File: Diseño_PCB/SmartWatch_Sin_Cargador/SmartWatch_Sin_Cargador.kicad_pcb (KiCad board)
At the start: 2 copper layers, 45 x 45 mm, 19 parts, among them J1 FTDI, J2 Input_BAT, J3 Input_Charger, SW1 SW_Push, SW2 SW_Push, SW3 SW_Push_Dual, SW4 SW_Push_Dual, SW5 SW_Push_Dual, SW6 SW_SPST, U1 ESP-12F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

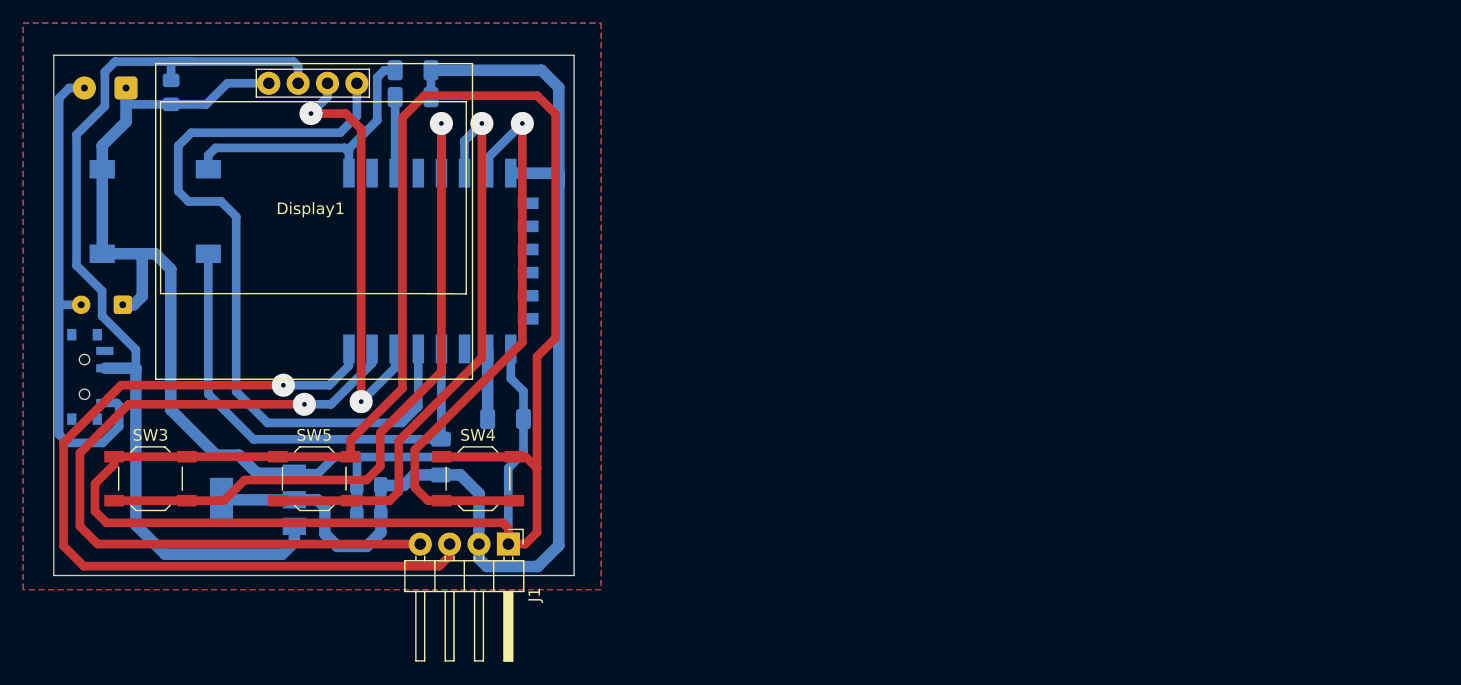
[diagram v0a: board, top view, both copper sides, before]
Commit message: Cree las carpetas de diseño 3D y actuaice el PCB del que no lleva cargador
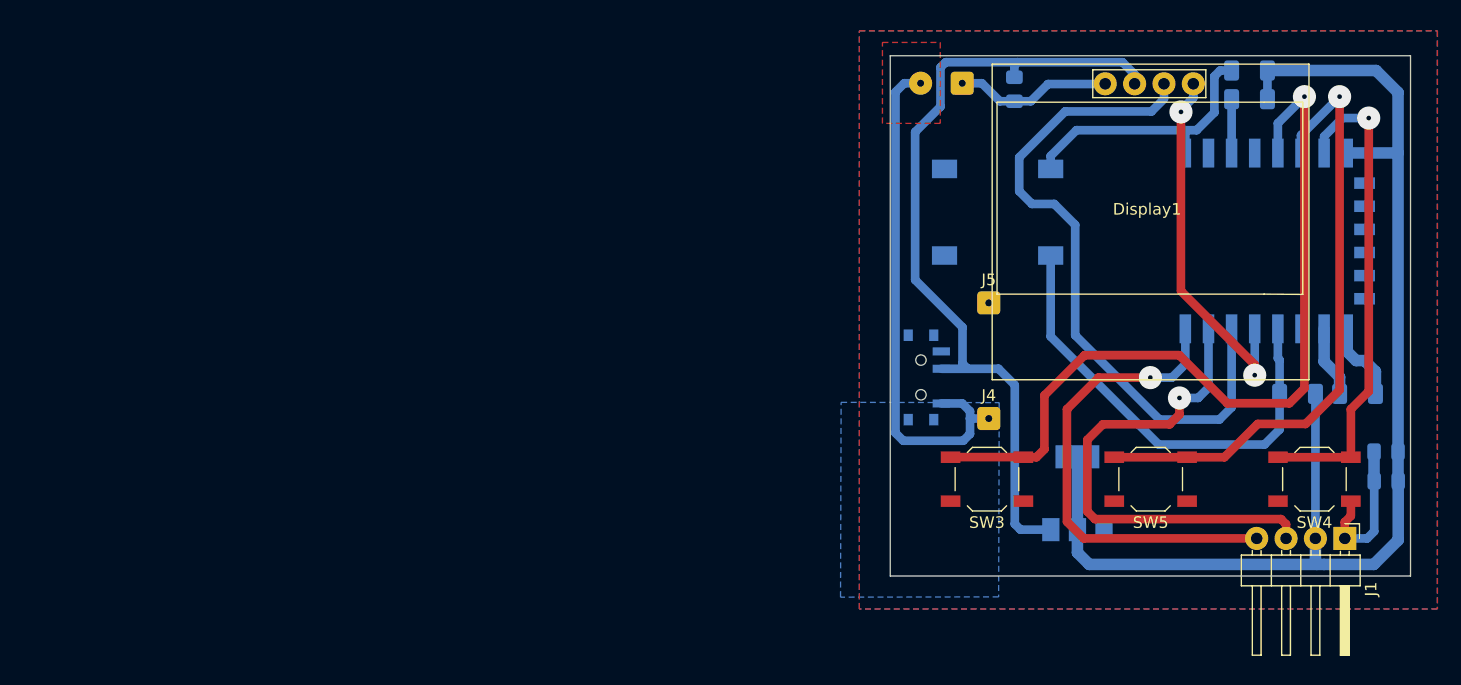
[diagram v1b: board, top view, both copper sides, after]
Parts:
- removed J3: Input_Charger, Connector_Wire:SolderWire-0.1sqmm_1x02_P3.6mm_D0.4mm_OD1mm
- added J4: Input_Charger++, Connector_Wire:SolderWire-0.1sqmm_1x01_D0.4mm_OD1mm, F.Cu at (164.5, 86.2)
- added J5: Input_Charger--, Connector_Wire:SolderWire-0.1sqmm_1x01_D0.4mm_OD1mm, F.Cu at (164.5, 76.2)
- moved C3 88.0 mm to (198.9, 91.6)
- moved C1 88.0 mm to (198.9, 89.1)
- moved R3 74.3 mm to (191.2, 84.1), turned to 180 degrees
- moved R4 73.7 mm to (196.4, 84.1)
- moved C2 72.9 mm to (166.7, 57.7)
- moved SW2 72.9 mm to (165.3, 72.1)
- moved SW1 72.9 mm to (165.3, 64.6)
- moved U1 72.4 mm to (185.0, 70.8)
- moved SW3 72.3 mm to (164.4, 91.4), turned to 180 degrees
- moved SW5 72.3 mm to (178.5, 91.4), turned to 180 degrees
- moved Display1 72.3 mm to (178.2, 67.8)
- moved SW4 72.3 mm to (192.7, 91.4), turned to 180 degrees
- moved J1 72.3 mm to (195.3, 96.6)
- moved R1 72.3 mm to (187.1, 58.6)
- moved SW6 72.3 mm to (159.0, 82.6)
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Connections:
- J1 pad 3: /Tx -> /Rx
- J1 pad 4: /Rx -> /Tx
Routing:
- net GND: track 267.2 -> 33.9 mm
- net /SDA: track 66.8 -> 32.3 mm, vias 0 -> 2
- net /Tx: track 73.3 -> 41.7 mm
- net /Rx: track 66.1 -> 43.3 mm
- net /SCL: track 37.5 -> 58.2 mm, vias 2 -> 0
- net /VCC_OLED: track 83.7 -> 70.8 mm
- net +3.3V: track 103.3 -> 113.8 mm
- net Net-(U1-GPIO14): track 60.4 -> 70.3 mm
- net Net-(U1-GPIO13): track 50.0 -> 42.2 mm
- net Net-(U1-GPIO12): track 50.5 -> 53.5 mm
- net /VBAT: track 42.9 -> 45.3 mm
- net Net-(U1-EN): track 6.58 -> 4.66 mm
- net Net-(U1-GPIO0): track 41.8 -> 40.0 mm
- net Net-(U1-~{RST}): track 24.9 -> 23.6 mm
- added copper zone on B.Cu, net /VBAT
- added copper zone on F.Cu, net /VBAT

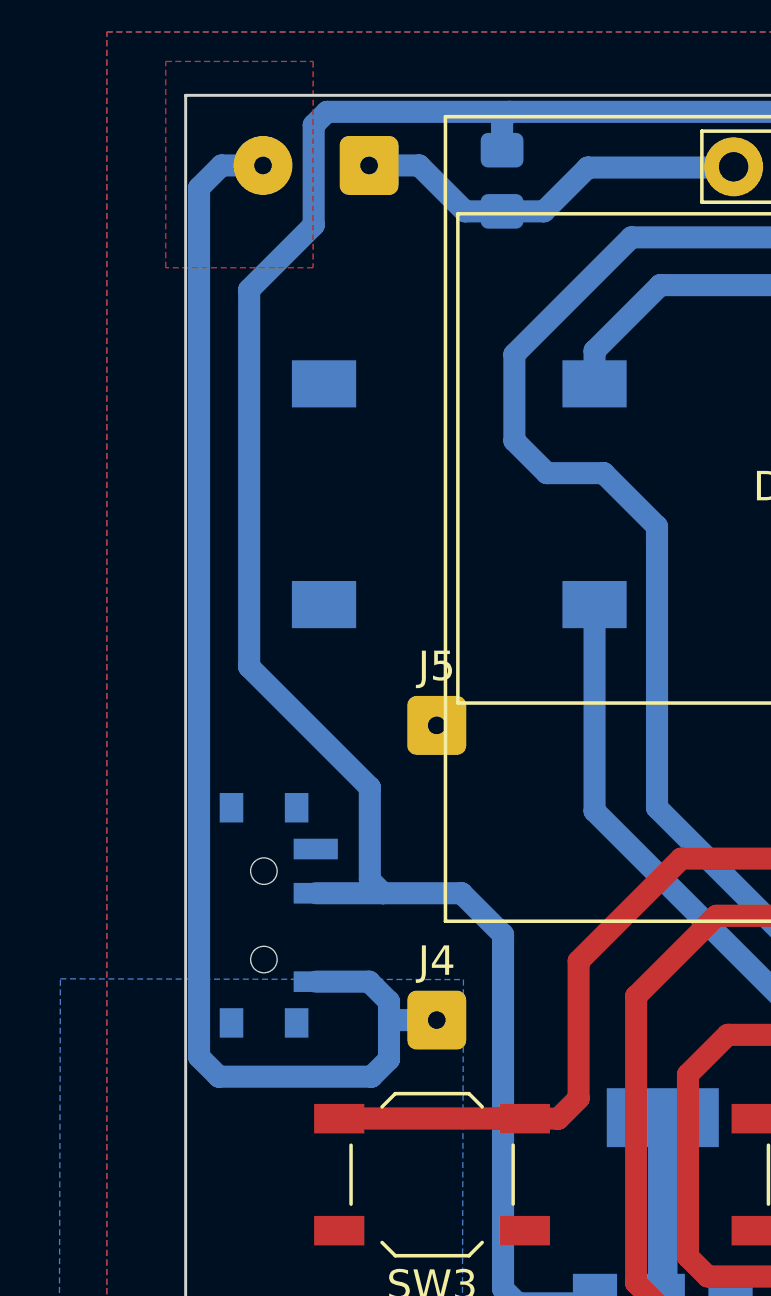
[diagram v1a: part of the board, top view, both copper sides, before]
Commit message: Arreglo PCB, Creacion de la carcasa 3D
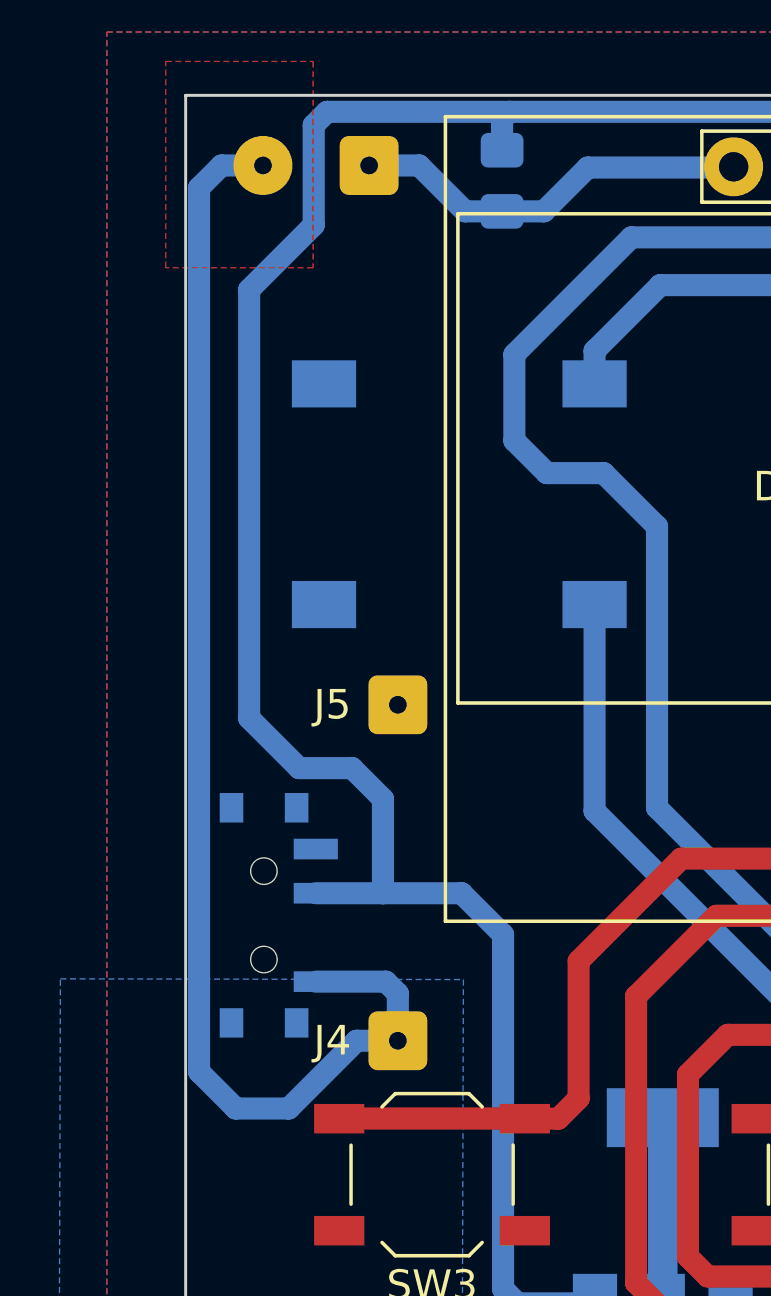
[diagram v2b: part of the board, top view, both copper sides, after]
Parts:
- moved J4 1.49 mm to (163.2, 86.9)
- moved J5 1.49 mm to (163.2, 75.5)
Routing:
- net /VCC_OLED: track 70.8 -> 71.8 mm
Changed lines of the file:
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@@
   )
   (footprint "Connector_Wire:SolderWire-0.1sqmm_1x01_D0.4mm_OD1mm" (layer "F.Cu")
-    (at 164.52 76.2)
+    (at 163.2 75.5)
     (descr "Soldered wire connection, for a single 0.1 mm² wire, basic insulation, conductor diameter 0.4mm, outer diameter 1mm, size source Multi-Contact FLEXI-E 0.1 (https://ec.staubli.com/AcroFiles/Catalogues/TM_Cab-Main-11014119_(en)_hi.pdf), bend radius 3 times outer diameter, generated with kicad-footprint-generator")
     (tags "connector wire 0.1sqmm")
@@
     (property "ki_keywords" "connector")
     (attr exclude_from_pos_files)
-    (fp_text reference "J5" (at 0 -2) (layer "F.SilkS")
+    (fp_text reference "J5" (at -2.22 0) (layer "F.SilkS")
         (effects (font (size 1 1) (thickness 0.15)))
     )
@@
   )
   (footprint "Connector_Wire:SolderWire-0.1sqmm_1x01_D0.4mm_OD1mm" (layer "F.Cu")
-    (at 164.52 86.2)
+    (at 163.2 86.9)
     (descr "Soldered wire connection, for a single 0.1 mm² wire, basic insulation, conductor diameter 0.4mm, outer diameter 1mm, size source Multi-Contact FLEXI-E 0.1 (https://ec.staubli.com/AcroFiles/Catalogues/TM_Cab-Main-11014119_(en)_hi.pdf), bend radius 3 times outer diameter, generated with kicad-footprint-generator")
     (tags "connector wire 0.1sqmm")
@@
     (property "ki_keywords" "connector")
     (attr exclude_from_pos_files)
-    (fp_text reference "J4" (at 0 -2) (layer "F.SilkS")
+    (fp_text reference "J4" (at -2.22 0) (layer "F.SilkS")
         (effects (font (size 1 1) (thickness 0.15)))
     )
@@
     (property "ki_keywords" "cap capacitor")
     (attr smd)
-    (fp_text reference "C3" (at 0 1.68) (layer "B.SilkS")
+    (fp_text reference "C3" (at 0 4.02) (layer "B.SilkS")
         (effects (font (size 1 1) (thickness 0.15)) (justify mirror))
     )
@@
     (property "ki_keywords" "linear regulator ldo fixed positive")
     (attr smd)
-    (fp_text reference "U2" (at 0 4.5 90) (layer "B.SilkS")
+    (fp_text reference "U2" (at 0 4.5) (layer "B.SilkS")
         (effects (font (size 1 1) (thickness 0.15)) (justify mirror))
     )
@@
     (property "ki_keywords" "connector")
     (attr exclude_from_pos_files)
-    (fp_text reference "J2" (at 1.8 2) (layer "B.SilkS")
+    (fp_text reference "J2" (at 1.8 -2.4) (layer "B.SilkS")
         (effects (font (size 1 1) (thickness 0.15)) (justify mirror))
     )
@@
     (property "ki_keywords" "cap capacitor")
     (attr smd)
-    (fp_text reference "C1" (at 0 1.68 -360) (layer "B.SilkS")
+    (fp_text reference "C1" (at 0 4.33 -360) (layer "B.SilkS")
         (effects (font (size 1 1) (thickness 0.15)) (justify mirror))
     )
@@
     (property "ki_keywords" "R res resistor")
     (attr smd)
-    (fp_text reference "R3" (at 0 1.82) (layer "B.SilkS")
+    (fp_text reference "R3" (at 0 -1.93 180) (layer "B.SilkS")
         (effects (font (size 1 1) (thickness 0.15)) (justify mirror))
     )
@@
     (property "ki_keywords" "cap capacitor")
     (attr smd)
-    (fp_text reference "C2" (at 0 1.68 -270) (layer "B.SilkS")
+    (fp_text reference "C2" (at -0.02 -1.7625 90) (layer "B.SilkS")
         (effects (font (size 1 1) (thickness 0.15)) (justify mirror))
     )
@@
     (property "ki_keywords" "802.11 Wi-Fi")
     (attr smd)
-    (fp_text reference "U1" (at -10.56 5.26 90) (layer "B.SilkS")
+    (fp_text reference "U1" (at 9.26 5.125 90) (layer "B.SilkS")
         (effects (font (size 1 1) (thickness 0.15)) (justify mirror))
     )
@@
     (property "ki_keywords" "R res resistor")
     (attr smd)
-    (fp_text reference "R4" (at 0 1.82) (layer "B.SilkS")
+    (fp_text reference "R4" (at -0.015 1.93 180) (layer "B.SilkS")
         (effects (font (size 1 1) (thickness 0.15)) (justify mirror))
     )
@@
     (property "ki_keywords" "R res resistor")
     (attr smd)
-    (fp_text reference "R1" (at 0 1.82) (layer "B.SilkS")
+    (fp_text reference "R1" (at 0.075 -1.92) (layer "B.SilkS")
         (effects (font (size 1 1) (thickness 0.15)) (justify mirror))
     )
@@
     (property "ki_keywords" "R res resistor")
     (attr smd)
-    (fp_text reference "R2" (at 0 1.82) (layer "B.SilkS")
+    (fp_text reference "R2" (at -3.425 0) (layer "B.SilkS")
         (effects (font (size 1 1) (thickness 0.15)) (justify mirror))
     )
@@
   (segment (start 192.775 98.695) (end 192.9 98.82) (width 1) (layer "B.Cu") (net 2))
   (segment (start 199.91 63.23) (end 199.92 63.22) (width 0.75) (layer "B.Cu") (net 2))
-  (segment (start 160.345 59.225) (end 158.155 61.415) (width 0.75) (layer "B.Cu") (net 3))
-  (segment (start 158.155 61.415) (end 158.155 74.21) (width 0.75) (layer "B.Cu") (net 3))
+  (segment (start 162.695 78.695) (end 162.695 81.895) (width 0.75) (layer "B.Cu") (net 3))
+  (segment (start 159.85 77.65) (end 161.65 77.65) (width 0.75) (layer "B.Cu") (net 3))
   (segment (start 166.77 95.32) (end 167.26 95.81) (width 0.75) (layer "B.Cu") (net 3))
   (segment (start 166.7375 55.6275) (end 166.985 55.38) (width 0.75) (layer "B.Cu") (net 3))
+  (segment (start 166.985 55.38) (end 160.795 55.38) (width 0.75) (layer "B.Cu") (net 3))
   (segment (start 177.135 57.245) (end 177.135 56.43) (width 0.75) (layer "B.Cu") (net 3))
   (segment (start 176.085 55.38) (end 166.985 55.38) (width 0.75) (layer "B.Cu") (net 3))
-  (segment (start 166.985 55.38) (end 160.795 55.38) (width 0.75) (layer "B.Cu") (net 3))
-  (segment (start 160.345 55.83) (end 160.345 59.225) (width 0.75) (layer "B.Cu") (net 3))
   (segment (start 166.77 83.3) (end 166.77 95.32) (width 0.75) (layer "B.Cu") (net 3))
-  (segment (start 158.155 74.21) (end 162.25 78.305) (width 0.75) (layer "B.Cu") (net 3))
+  (segment (start 158.155 61.415) (end 158.155 75.955) (width 0.75) (layer "B.Cu") (net 3))
+  (segment (start 160.795 55.38) (end 160.345 55.83) (width 0.75) (layer "B.Cu") (net 3))
+  (segment (start 160.345 59.225) (end 158.155 61.415) (width 0.75) (layer "B.Cu") (net 3))
   (segment (start 160.415 81.895) (end 162.695 81.895) (width 0.75) (layer "B.Cu") (net 3))
   (segment (start 162.695 81.895) (end 165.365 81.895) (width 0.75) (layer "B.Cu") (net 3))
-  (segment (start 162.25 78.305) (end 162.25 81.45) (width 0.75) (layer "B.Cu") (net 3))
-  (segment (start 160.795 55.38) (end 160.345 55.83) (width 0.75) (layer "B.Cu") (net 3))
-  (segment (start 162.25 81.45) (end 162.695 81.895) (width 0.75) (layer "B.Cu") (net 3))
+  (segment (start 158.155 75.955) (end 159.85 77.65) (width 0.75) (layer "B.Cu") (net 3))
   (segment (start 177.135 56.43) (end 176.085 55.38) (width 0.75) (layer "B.Cu") (net 3))
   (segment (start 166.7375 56.6825) (end 166.7375 55.6275) (width 0.75) (layer "B.Cu") (net 3))
+  (segment (start 161.65 77.65) (end 162.695 78.695) (width 0.75) (layer "B.Cu") (net 3))
   (segment (start 165.365 81.895) (end 166.77 83.3) (width 0.75) (layer "B.Cu") (net 3))
   (segment (start 167.26 95.81) (end 169.89 95.81) (width 0.75) (layer "B.Cu") (net 3))
+  (segment (start 160.345 55.83) (end 160.345 59.225) (width 0.75) (layer "B.Cu") (net 3))
   (segment (start 167.155 63.61) (end 171.125 59.64) (width 0.75) (layer "B.Cu") (net 4))
   (segment (start 179.29 86.29) (end 171.995 78.995) (width 0.75) (layer "B.Cu") (net 4))
@@
   (segment (start 181.525 81.5) (end 180.365 82.66) (width 0.75) (layer "B.Cu") (net 7))
   (segment (start 181.525 78.44) (end 181.525 81.5) (width 0.75) (layer "B.Cu") (net 7))
-  (segment (start 162.9 86.2) (end 162.9 85.57) (width 0.75) (layer "B.Cu") (net 8))
+  (segment (start 163.2 85.3) (end 162.795 84.895) (width 0.75) (layer "B.Cu") (net 8))
+  (segment (start 156.455 87.955) (end 157.7 89.2) (width 0.75) (layer "B.Cu") (net 8))
+  (segment (start 157.7 89.2) (end 159.5 89.2) (width 0.75) (layer "B.Cu") (net 8))
+  (segment (start 159.5 89.2) (end 161.8 86.9) (width 0.75) (layer "B.Cu") (net 8))
   (segment (start 157.215 57.2) (end 156.455 57.96) (width 0.75) (layer "B.Cu") (net 8))
-  (segment (start 156.455 57.96) (end 156.455 87.45) (width 0.75) (layer "B.Cu") (net 8))
+  (segment (start 162.795 84.895) (end 160.415 84.895) (width 0.75) (layer "B.Cu") (net 8))
   (segment (start 158.625 57.2) (end 157.215 57.2) (width 0.75) (layer "B.Cu") (net 8))
-  (segment (start 162.31 88.12) (end 162.9 87.53) (width 0.75) (layer "B.Cu") (net 8))
-  (segment (start 157.125 88.12) (end 162.31 88.12) (width 0.75) (layer "B.Cu") (net 8))
-  (segment (start 162.9 85.57) (end 162.225 84.895) (width 0.75) (layer "B.Cu") (net 8))
-  (segment (start 156.455 87.45) (end 157.125 88.12) (width 0.75) (layer "B.Cu") (net 8))
-  (segment (start 164.52 86.2) (end 162.9 86.2) (width 0.75) (layer "B.Cu") (net 8))
-  (segment (start 162.9 87.53) (end 162.9 86.2) (width 0.75) (layer "B.Cu") (net 8))
-  (segment (start 162.225 84.895) (end 160.415 84.895) (width 0.75) (layer "B.Cu") (net 8))
+  (segment (start 161.8 86.9) (end 163.2 86.9) (width 0.75) (layer "B.Cu") (net 8))
+  (segment (start 156.455 57.96) (end 156.455 87.955) (width 0.75) (layer "B.Cu") (net 8))
+  (segment (start 163.2 86.9) (end 163.2 85.3) (width 0.75) (layer "B.Cu") (net 8))
   (segment (start 185.525 63.24) (end 185.525 58.58) (width 0.75) (layer "B.Cu") (net 9))
   (segment (start 172.105 61.26) (end 181.425 61.26) (width 0.75) (layer "B.Cu") (net 10))
